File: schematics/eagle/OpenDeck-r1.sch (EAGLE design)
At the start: 248 parts, among them U1 ATMEGA32U4-AU, U2 4067D, U3 4067D, U4 74AC11238D, U5 ULN2803, U6 74AC165D, U7 74AC11238D, U8 6N138, Y1 16MHz

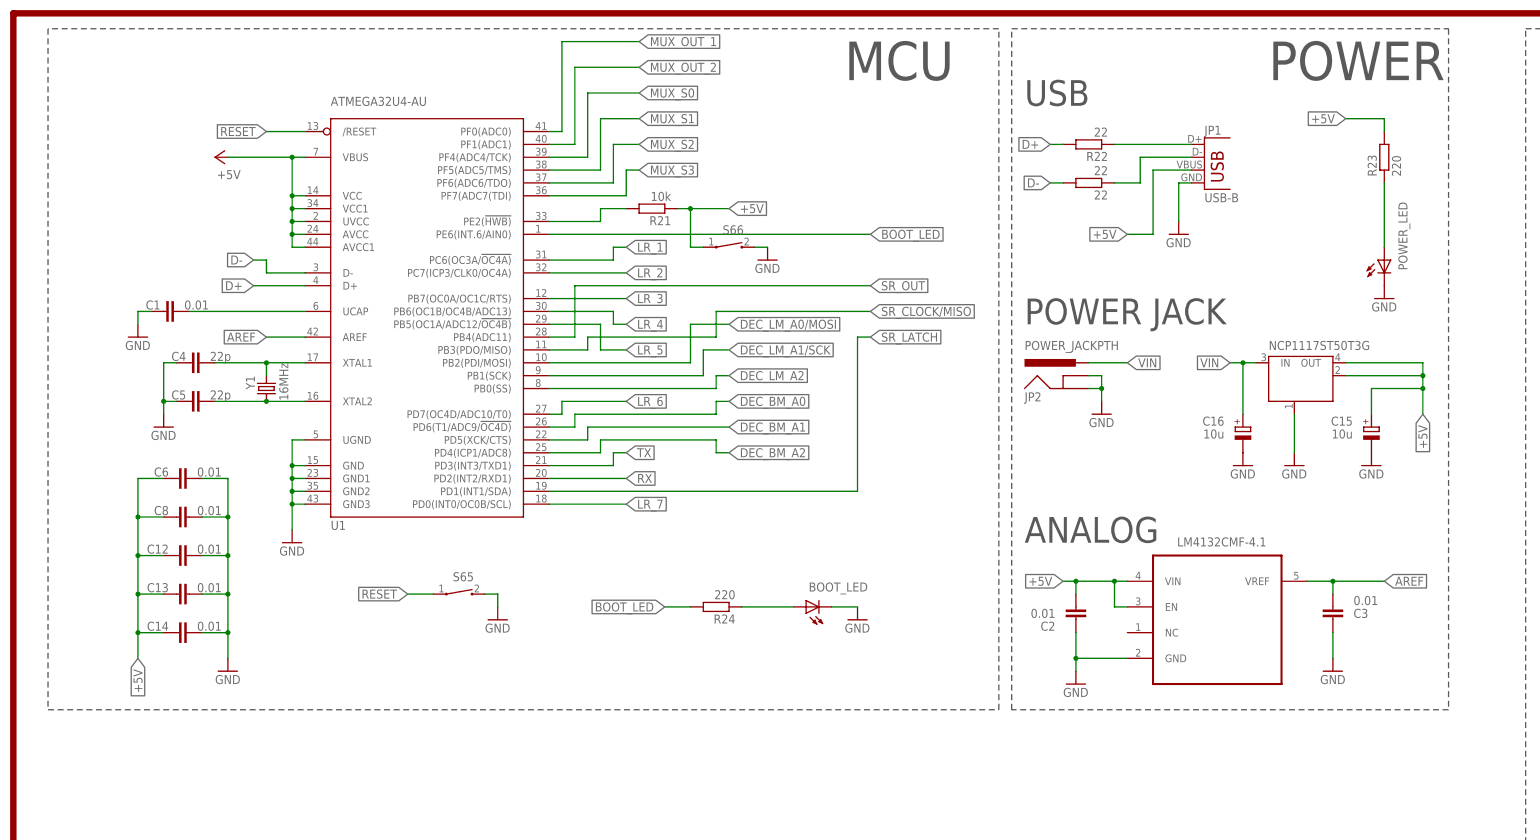
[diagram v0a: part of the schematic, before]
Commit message: add decoupling cap to VBUS
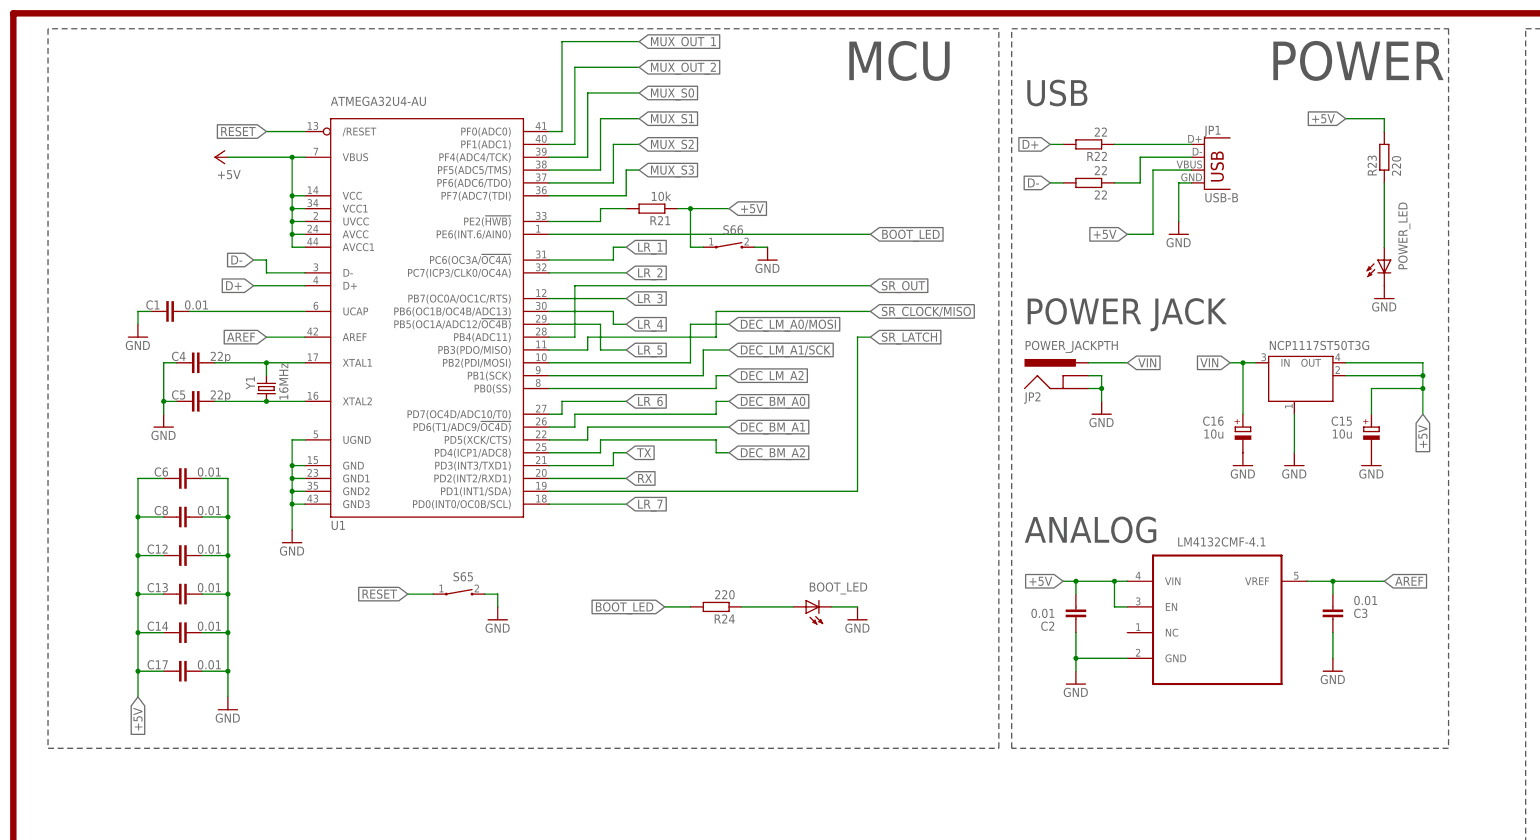
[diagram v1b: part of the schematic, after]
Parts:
- added C17: 0.01, rcl:C-EU025-025X050
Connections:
- net +5V: now also C17.1
- net GND: now also C17.2
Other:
- note added: "VBUS"
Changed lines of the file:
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@@
 <setting verticaltext="up"/>
 </settings>
-<grid distance="0.1" unitdist="inch" unit="inch" style="lines" multiple="1" display="no" altdistance="0.01" altunitdist="inch" altunit="inch"/>
+<grid distance="0.1" unitdist="inch" unit="inch" style="lines" multiple="1" display="yes" altdistance="0.01" altunitdist="inch" altunit="inch"/>
 <layers>
 <layer number="1" name="Top" color="4" fill="1" visible="no" active="no"/>
@@
 <part name="C16" library="rcl" deviceset="CPOL-EU" device="SMCB" value="10u"/>
 <part name="GND29" library="supply1" deviceset="GND" device=""/>
+<part name="C17" library="rcl" deviceset="C-EU" device="025-025X050" value="0.01"/>
 </parts>
 <sheets>
@@
 <text x="200.66" y="347.98" size="5.08" layer="97" font="vector">USB</text>
 <wire x1="195.58" y1="363.22" x2="7.62" y2="363.22" width="0.1524" layer="97" style="dashdot"/>
-<wire x1="7.62" y1="363.22" x2="7.62" y2="228.6" width="0.1524" layer="97" style="dashdot"/>
-<wire x1="7.62" y1="228.6" x2="195.58" y2="228.6" width="0.1524" layer="97" style="dashdot"/>
-<wire x1="195.58" y1="228.6" x2="195.58" y2="363.22" width="0.1524" layer="97" style="dashdot"/>
+<wire x1="7.62" y1="363.22" x2="7.62" y2="220.98" width="0.1524" layer="97" style="dashdot"/>
+<wire x1="7.62" y1="220.98" x2="195.58" y2="220.98" width="0.1524" layer="97" style="dashdot"/>
+<wire x1="195.58" y1="220.98" x2="195.58" y2="363.22" width="0.1524" layer="97" style="dashdot"/>
 <text x="165.1" y="353.06" size="7.62" layer="97" font="vector">MCU</text>
 <wire x1="198.12" y1="363.22" x2="284.48" y2="363.22" width="0.1524" layer="97" style="dashdot"/>
-<wire x1="284.48" y1="363.22" x2="284.48" y2="228.6" width="0.1524" layer="97" style="dashdot"/>
-<wire x1="284.48" y1="228.6" x2="198.12" y2="228.6" width="0.1524" layer="97" style="dashdot"/>
-<wire x1="198.12" y1="228.6" x2="198.12" y2="363.22" width="0.1524" layer="97" style="dashdot"/>
+<wire x1="284.48" y1="363.22" x2="284.48" y2="220.98" width="0.1524" layer="97" style="dashdot"/>
+<wire x1="284.48" y1="220.98" x2="198.12" y2="220.98" width="0.1524" layer="97" style="dashdot"/>
+<wire x1="198.12" y1="220.98" x2="198.12" y2="363.22" width="0.1524" layer="97" style="dashdot"/>
 <text x="248.92" y="353.06" size="7.62" layer="97" font="vector">POWER</text>
 <text x="154.94" y="190.5" size="7.62" layer="97" font="vector">MULTIPLEXING</text>
@@
 <text x="304.8" y="152.4" size="2.54" layer="104" font="vector">U2 POWER</text>
 <text x="332.74" y="152.4" size="2.54" layer="104" font="vector">U3 POWER</text>
-<text x="12.7" y="274.32" size="2.54" layer="104" font="vector">VCC</text>
-<text x="12.7" y="266.7" size="2.54" layer="104" font="vector">VCC1</text>
-<text x="12.7" y="259.08" size="2.54" layer="104" font="vector">UVCC</text>
-<text x="12.7" y="251.46" size="2.54" layer="104" font="vector">AVCC</text>
-<text x="12.7" y="243.84" size="2.54" layer="104" font="vector">AVCC1</text>
+<text x="12.7" y="266.7" size="2.54" layer="104" font="vector">VCC</text>
+<text x="12.7" y="259.08" size="2.54" layer="104" font="vector">VCC1</text>
+<text x="12.7" y="251.46" size="2.54" layer="104" font="vector">UVCC</text>
+<text x="12.7" y="243.84" size="2.54" layer="104" font="vector">AVCC</text>
+<text x="12.7" y="236.22" size="2.54" layer="104" font="vector">AVCC1</text>
 <text x="530.86" y="73.66" size="7.62" layer="97" font="vector">Note:
 All diodes 1N4148</text>
 <text x="200.66" y="304.8" size="5.08" layer="97" font="vector">POWER JACK</text>
+<text x="12.7" y="274.32" size="2.54" layer="104" font="vector">VBUS</text>
 </plain>
 <instances>
@@
 <attribute name="VALUE" x="37.084" y="245.999" size="1.778" layer="96" font="vector" rot="MR180"/>
 </instance>
-<instance part="GND22" gate="1" x="43.18" y="236.22" smashed="yes">
-<attribute name="VALUE" x="40.64" y="233.68" size="1.778" layer="96" font="vector"/>
+<instance part="GND22" gate="1" x="43.18" y="228.6" smashed="yes">
+<attribute name="VALUE" x="40.64" y="226.06" size="1.778" layer="96" font="vector"/>
 </instance>
 <instance part="JP2" gate="G$1" x="210.82" y="289.56"/>
@@
 <attribute name="VALUE" x="241.3" y="274.32" size="1.778" layer="96" font="vector"/>
 </instance>
+<instance part="C17" gate="G$1" x="33.02" y="236.22" smashed="yes" rot="MR270">
+<attribute name="NAME" x="31.496" y="236.601" size="1.778" layer="95" font="vector" rot="MR0"/>
+<attribute name="VALUE" x="37.084" y="238.379" size="1.778" layer="96" font="vector" rot="MR180"/>
+</instance>
 </instances>
 <busses>
@@
 <junction x="43.18" y="259.08"/>
 <junction x="43.18" y="251.46"/>
-<wire x1="43.18" y1="243.84" x2="43.18" y2="238.76" width="0.1524" layer="91"/>
+<wire x1="43.18" y1="243.84" x2="43.18" y2="236.22" width="0.1524" layer="91"/>
 <junction x="43.18" y="243.84"/>
 <pinref part="GND22" gate="1" pin="GND"/>
+<pinref part="C17" gate="G$1" pin="2"/>
+<wire x1="43.18" y1="236.22" x2="43.18" y2="231.14" width="0.1524" layer="91"/>
+<wire x1="38.1" y1="236.22" x2="43.18" y2="236.22" width="0.1524" layer="91"/>
+<junction x="43.18" y="236.22"/>
 </segment>
 <segment>
@@
 <junction x="25.4" y="251.46"/>
 <junction x="25.4" y="243.84"/>
-<wire x1="25.4" y1="243.84" x2="25.4" y2="238.76" width="0.1524" layer="91"/>
-<label x="25.4" y="238.76" size="1.778" layer="95" font="vector" rot="MR270" xref="yes"/>
+<wire x1="25.4" y1="243.84" x2="25.4" y2="236.22" width="0.1524" layer="91"/>
+<label x="25.4" y="231.14" size="1.778" layer="95" font="vector" rot="MR270" xref="yes"/>
+<pinref part="C17" gate="G$1" pin="1"/>
+<wire x1="25.4" y1="236.22" x2="25.4" y2="231.14" width="0.1524" layer="91"/>
+<wire x1="30.48" y1="236.22" x2="25.4" y2="236.22" width="0.1524" layer="91"/>
+<junction x="25.4" y="236.22"/>
 </segment>
 <segment>

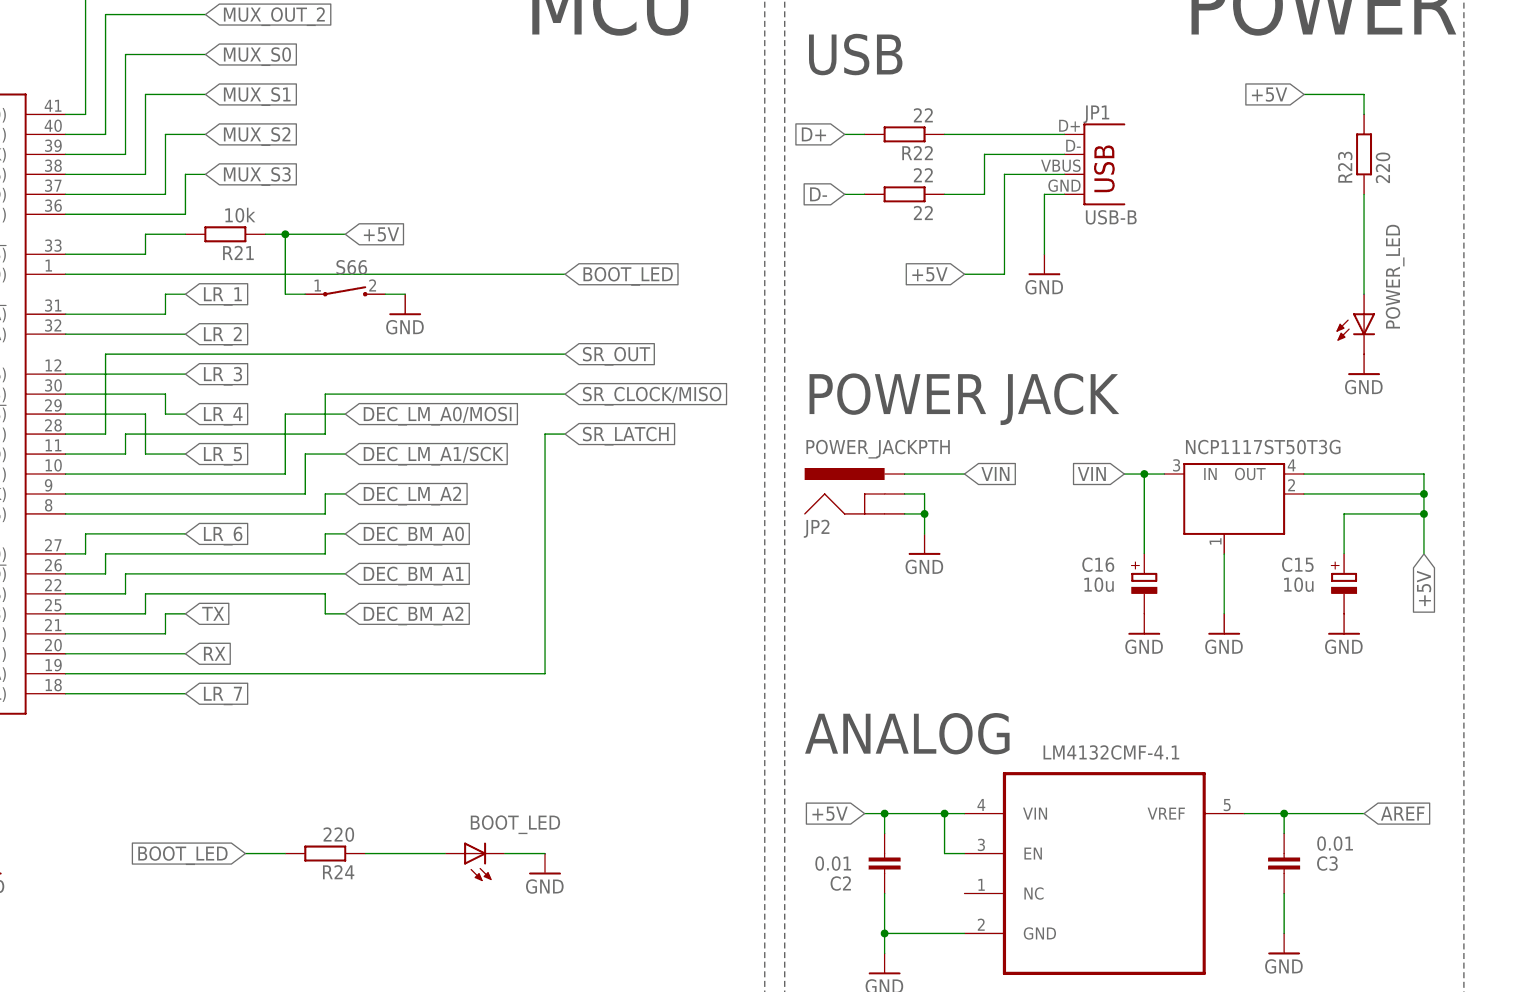
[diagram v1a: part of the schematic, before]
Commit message: fix HWBE button, lower LED resistor values
* lower BOOT_LED and POWER_LED resistor values from 220 to 130

* fix incorrect HWBE switch placement
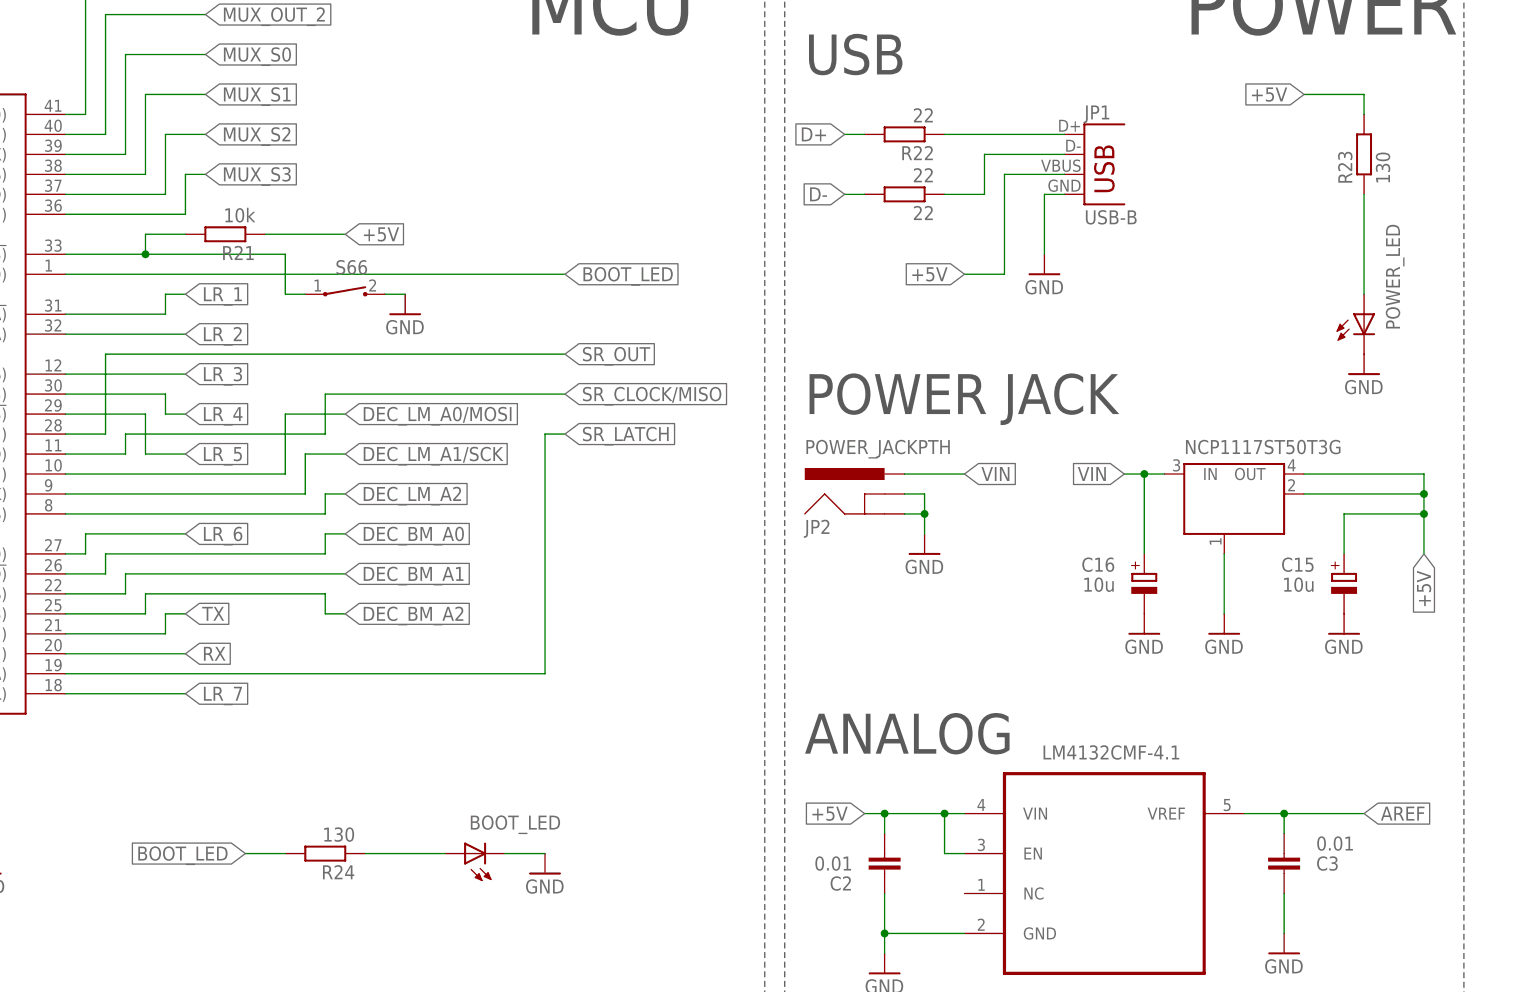
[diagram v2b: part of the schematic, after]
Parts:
- R23, R24: value 220 -> 130
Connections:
- removed net N$74: R21.2, U1.PE2(!HWB)
- new net N$77: R21.2, S66.1, U1.PE2(!HWB)
- net +5V: no longer S66.1
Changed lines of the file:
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@@
 <setting verticaltext="up"/>
 </settings>
-<grid distance="0.1" unitdist="inch" unit="inch" style="lines" multiple="1" display="yes" altdistance="0.01" altunitdist="inch" altunit="inch"/>
+<grid distance="0.1" unitdist="inch" unit="inch" style="lines" multiple="1" display="no" altdistance="0.01" altunitdist="inch" altunit="inch"/>
 <layers>
 <layer number="1" name="Top" color="4" fill="1" visible="no" active="no"/>
@@
 <part name="JP2" library="SparkFun-Connectors" deviceset="POWER_JACK" device="PTH"/>
 <part name="GND24" library="supply1" deviceset="GND" device=""/>
-<part name="R23" library="rcl" deviceset="R-EU_" device="0204/7" value="220"/>
+<part name="R23" library="rcl" deviceset="R-EU_" device="0204/7" value="130"/>
 <part name="GND25" library="supply1" deviceset="GND" device=""/>
-<part name="R24" library="rcl" deviceset="R-EU_" device="0204/7" value="220"/>
+<part name="R24" library="rcl" deviceset="R-EU_" device="0204/7" value="130"/>
 <part name="GND26" library="supply1" deviceset="GND" device=""/>
 <part name="BOOT_LED" library="led" deviceset="*W51M" device="" technology="LA"/>
@@
 </segment>
 </net>
-<net name="N$74" class="0">
-<segment>
-<pinref part="U1" gate="G$1" pin="PE2(!HWB)"/>
-<wire x1="106.68" y1="325.12" x2="116.84" y2="325.12" width="0.1524" layer="91"/>
-<wire x1="116.84" y1="325.12" x2="116.84" y2="327.66" width="0.1524" layer="91"/>
-<wire x1="116.84" y1="327.66" x2="121.92" y2="327.66" width="0.1524" layer="91"/>
-<pinref part="R21" gate="G$1" pin="2"/>
-</segment>
-</net>
 <net name="RESET" class="0">
 <segment>
@@
 <segment>
 <pinref part="R21" gate="G$1" pin="1"/>
-<wire x1="132.08" y1="327.66" x2="134.62" y2="327.66" width="0.1524" layer="91"/>
 <label x="142.24" y="327.66" size="1.778" layer="95" font="vector" xref="yes"/>
-<pinref part="S66" gate="G$1" pin="1"/>
-<wire x1="134.62" y1="327.66" x2="142.24" y2="327.66" width="0.1524" layer="91"/>
-<wire x1="137.16" y1="320.04" x2="134.62" y2="320.04" width="0.1524" layer="91"/>
-<wire x1="134.62" y1="320.04" x2="134.62" y2="327.66" width="0.1524" layer="91"/>
-<junction x="134.62" y="327.66"/>
+<wire x1="132.08" y1="327.66" x2="142.24" y2="327.66" width="0.1524" layer="91"/>
 </segment>
 <segment>
@@
 </segment>
 </net>
+<net name="N$77" class="1">
+<segment>
+<pinref part="S66" gate="G$1" pin="1"/>
+<wire x1="137.16" y1="320.04" x2="134.62" y2="320.04" width="0.1524" layer="91"/>
+<wire x1="134.62" y1="320.04" x2="134.62" y2="325.12" width="0.1524" layer="91"/>
+<pinref part="U1" gate="G$1" pin="PE2(!HWB)"/>
+<wire x1="106.68" y1="325.12" x2="116.84" y2="325.12" width="0.1524" layer="91"/>
+<wire x1="116.84" y1="325.12" x2="116.84" y2="327.66" width="0.1524" layer="91"/>
+<wire x1="116.84" y1="327.66" x2="121.92" y2="327.66" width="0.1524" layer="91"/>
+<pinref part="R21" gate="G$1" pin="2"/>
+<wire x1="134.62" y1="325.12" x2="116.84" y2="325.12" width="0.1524" layer="91"/>
+<junction x="116.84" y="325.12"/>
+</segment>
+</net>
